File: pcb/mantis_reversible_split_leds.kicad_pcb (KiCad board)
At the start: 2 copper layers, 111 x 130.6 mm, 79 parts

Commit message: pcb: Remove duplicate pads
Replace reversible switch footprint to remove duplicate pads.

Signed-off-by: Felix Kuehling <felix.kuehling@gmail.com>
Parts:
- S1, S10, S11, S12, S2, S3, S4, S5, S6, S7, S8, S9: footprint PG1350 -> Mantis:PG1350-reversible

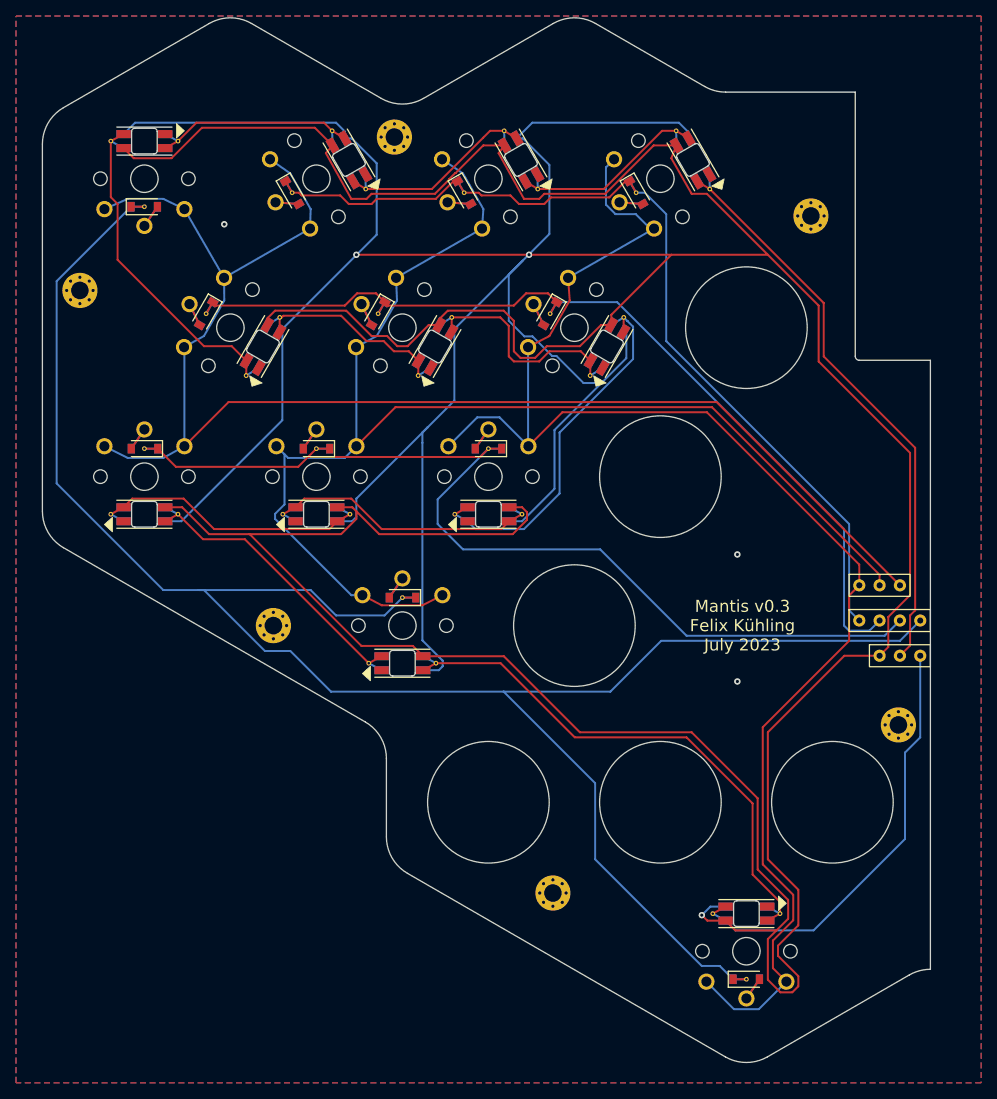
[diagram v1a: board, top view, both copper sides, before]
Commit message: pcb: Minor fixes and cleanups
Fix DRC warnings about silk screen intsecting edge cuts or solder mask.
Minor routing cleanups.

Signed-off-by: Felix Kuehling <felix.kuehling@gmail.com>
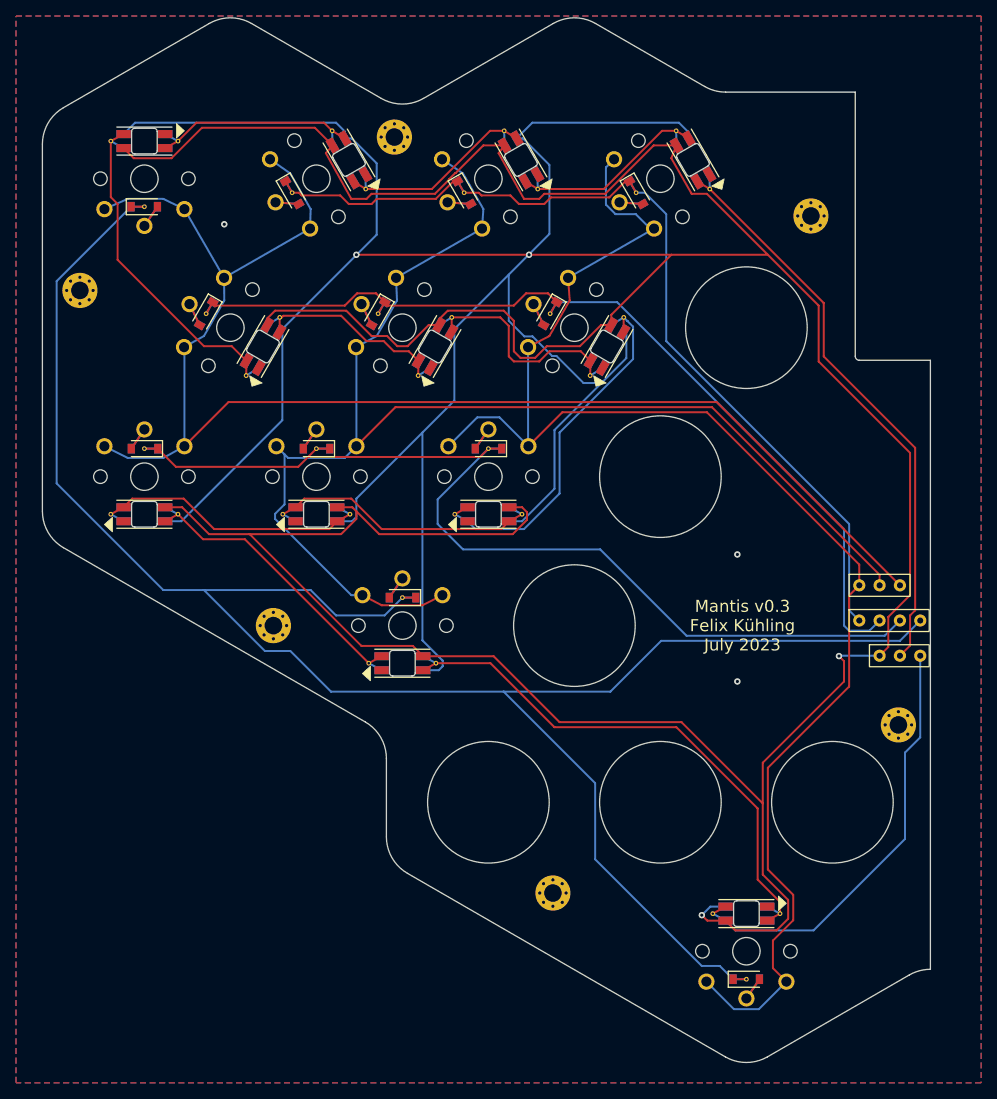
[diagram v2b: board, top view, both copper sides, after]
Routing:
- net VCC: track 781.3 -> 741.1 mm, vias 3 -> 4
- net RT: track 247.7 -> 247.0 mm
- net C3: track 186.4 -> 185.8 mm

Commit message: pcb: Generated Gerber files for v0.3
Signed-off-by: Felix Kuehling <felix.kuehling@gmail.com>
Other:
- rule pad_to_mask_clearance: 0.05 -> 0
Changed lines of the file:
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@@
   )
   (setup
-    (pad_to_mask_clearance 0.05)
+    (stackup
+      (layer "F.SilkS" (type "Top Silk Screen"))
+      (layer "F.Paste" (type "Top Solder Paste"))
+      (layer "F.Mask" (type "Top Solder Mask") (thickness 0.01))
+      (layer "F.Cu" (type "copper") (thickness 0.035))
+      (layer "dielectric 1" (type "core") (thickness 1.51) (material "FR4") (epsilon_r 4.5) (loss_tangent 0.02))
+      (layer "B.Cu" (type "copper") (thickness 0.035))
+      (layer "B.Mask" (type "Bottom Solder Mask") (thickness 0.01))
+      (layer "B.Paste" (type "Bottom Solder Paste"))
+      (layer "B.SilkS" (type "Bottom Silk Screen"))
+      (copper_finish "None")
+      (dielectric_constraints no)
+    )
+    (pad_to_mask_clearance 0)
     (pcbplotparams
       (layerselection 0x00010fc_ffffffff)
@@
       (outputformat 1)
       (mirror false)
-      (drillshape 1)
+      (drillshape 0)
       (scaleselection 1)
-      (outputdirectory "")
+      (outputdirectory "gerber/")
     )
   )
